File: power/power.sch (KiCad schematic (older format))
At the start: 14 parts, among them P1 CONN_2, P2 CONN_5X2, U1 KPS-5, U2 RB-0515S, U3 RB-0515S, U4 RB-0512D, U5 RB-0505D

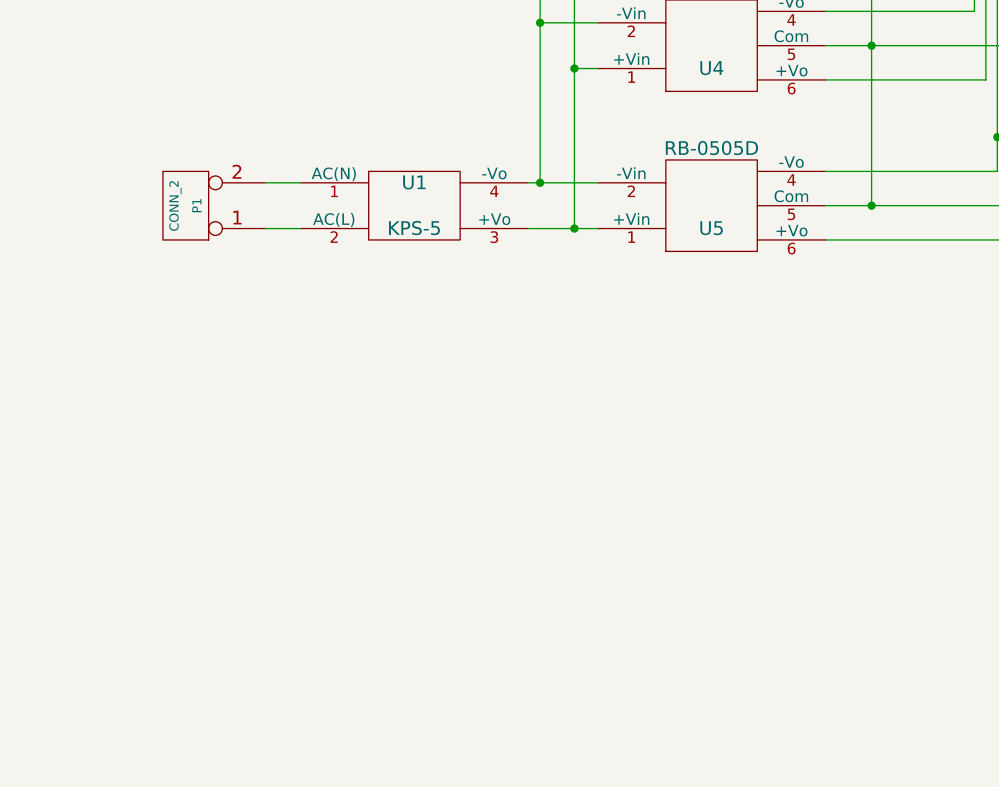
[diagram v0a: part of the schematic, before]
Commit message: [libs, power] dc-dc convertors
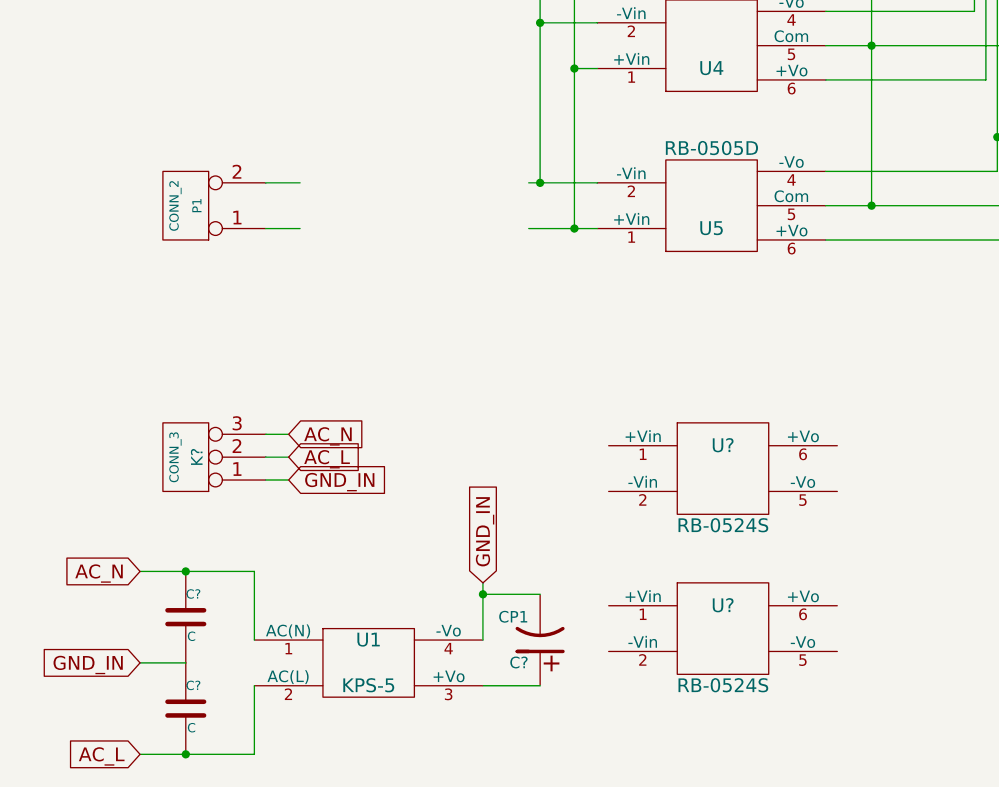
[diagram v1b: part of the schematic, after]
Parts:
- added C? (x2): C, ~, symbol C
- added C?: CP1, ~, symbol CP1
- added K?: CONN_3, ~, symbol CONN_3
- added U? (x2): RB-0524S, ~, symbol RB-0524S
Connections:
- net labels added: AC_L, AC_N, GND_IN
- wire segments 50 -> 61
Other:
- moved on the sheet: U1
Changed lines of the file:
@@
 LIBS:ad8421
 LIBS:ad8067
+LIBS:rb-0524s
 LIBS:power-cache
 EELAYER 27 0
@@
 Sheet 1 1
 Title "Power for PID controller"
-Date "28 jan 2014"
+Date "2 apr 2014"
 Rev ""
 Comp "MIT BEC5"
@@
 L KPS-5 U1
 U 1 1 52E78312
-P 3900 4900
-F 0 "U1" H 3900 5000 60  0000 C CNN
-F 1 "KPS-5" H 3900 4800 60  0000 C CNN
-F 2 "~" H 3900 4900 60  0000 C CNN
-F 3 "~" H 3900 4900 60  0000 C CNN
-	1    3900 4900
+P 3700 6900
+F 0 "U1" H 3700 7000 60  0000 C CNN
+F 1 "KPS-5" H 3700 6800 60  0000 C CNN
+F 2 "~" H 3700 6900 60  0000 C CNN
+F 3 "~" H 3700 6900 60  0000 C CNN
+	1    3700 6900
 	1    0    0    -1
 $EndComp
@@
 NoConn ~ 8400 3900
 NoConn ~ 8400 4000
+$Comp
+L CONN_3 K?
+U 1 1 533AD55D
+P 2900 6000
+F 0 "K?" V 2850 6000 50  0000 C CNN
+F 1 "CONN_3" V 2950 6000 40  0000 C CNN
+F 2 "~" H 2900 6000 60  0000 C CNN
+F 3 "~" H 2900 6000 60  0000 C CNN
+	1    2900 6000
+	-1   0    0    1
+$EndComp
+Text GLabel 3350 5900 2    60   Input ~ 0
+AC_N
+Text GLabel 3350 6000 2    60   Input ~ 0
+AC_L
+Text GLabel 3350 6100 2    60   Input ~ 0
+GND_IN
+Wire Wire Line
+	3250 5900 3350 5900
+Wire Wire Line
+	3250 6000 3350 6000
+Wire Wire Line
+	3250 6100 3350 6100
+Text GLabel 2700 6500 0    60   Input ~ 0
+AC_N
+Text GLabel 2700 7300 0    60   Input ~ 0
+AC_L
+Text GLabel 2700 6900 0    60   Input ~ 0
+GND_IN
+$Comp
+L C C?
+U 1 1 533AD679
+P 2900 6700
+F 0 "C?" H 2900 6800 40  0000 L CNN
+F 1 "C" H 2906 6615 40  0000 L CNN
+F 2 "~" H 2938 6550 30  0000 C CNN
+F 3 "~" H 2900 6700 60  0000 C CNN
+	1    2900 6700
+	1    0    0    -1
+$EndComp
+$Comp
+L C C?
+U 1 1 533AD688
+P 2900 7100
+F 0 "C?" H 2900 7200 40  0000 L CNN
+F 1 "C" H 2906 7015 40  0000 L CNN
+F 2 "~" H 2938 6950 30  0000 C CNN
+F 3 "~" H 2900 7100 60  0000 C CNN
+	1    2900 7100
+	1    0    0    -1
+$EndComp
+Wire Wire Line
+	2700 6900 2900 6900
+Wire Wire Line
+	2700 6500 3200 6500
+Wire Wire Line
+	2700 7300 3200 7300
+Wire Wire Line
+	3200 6500 3200 6800
+Connection ~ 2900 6500
+Wire Wire Line
+	3200 7300 3200 7000
+Connection ~ 2900 7300
+Text GLabel 4200 6550 1    60   Input ~ 0
+GND_IN
+Wire Wire Line
+	4200 6550 4200 6800
+Wire Wire Line
+	4200 7000 4450 7000
+Wire Wire Line
+	4450 6600 4200 6600
+Connection ~ 4200 6600
+$Comp
+L CP1 C?
+U 1 1 533AD9CB
+P 4450 6800
+F 0 "C?" H 4500 6900 50  0000 L CNN
+F 1 "CP1" H 4500 6700 50  0000 L CNN
+F 2 "~" H 4450 6800 60  0000 C CNN
+F 3 "~" H 4450 6800 60  0000 C CNN
+	1    4450 6800
+	-1   0    0    1
+$EndComp
+$Comp
+L RB-0524S U?
+U 1 1 533B760A
+P 5250 6050
+F 0 "U?" H 5250 6150 60  0000 C CNN
+F 1 "RB-0524S" H 5250 5800 60  0000 C CNN
+F 2 "~" H 5250 6050 60  0000 C CNN
+F 3 "~" H 5250 6050 60  0000 C CNN
+	1    5250 6050
+	1    0    0    -1
+$EndComp
+$Comp
+L RB-0524S U?
+U 1 1 533B7617
+P 5250 6750
+F 0 "U?" H 5250 6850 60  0000 C CNN
+F 1 "RB-0524S" H 5250 6500 60  0000 C CNN
+F 2 "~" H 5250 6750 60  0000 C CNN
+F 3 "~" H 5250 6750 60  0000 C CNN
+	1    5250 6750
+	1    0    0    -1
+$EndComp
 $EndSCHEMATC

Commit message: [power] new design
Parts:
- removed C1, C2, C3, C4, C5, C6, C7: CP1, ~, symbol CP1
- removed P1: CONN_2, ~, symbol CONN_2
- removed U2, U3: RB-0515S, ~, symbol RB-0515S
- removed U4: RB-0512D, ~, symbol RB-0512D
- removed U5: RB-0505D, ~, symbol RB-0505D
- removed U? (x2): RB-0524S, ~, symbol RB-0524S
- added C? (x6): 0.022uF, ~, symbol C
- added C? (x9): 330uF, ~, symbol CP1
- added C?: 10uF, ~, symbol CP1
- added C? (x4): 10uF, ~, symbol C
- added C? (x9): C, ~, symbol C
- added C? (x8): 0.01uF, ~, symbol C
- added L? (x14): 10uH, ~, symbol INDUCTOR
- added L? (x5): 470uH, ~, symbol INDUCTOR
- added L? (x5): CIM21J252, ~, symbol INDUCTOR
- added R?: R, ~, symbol R
- added R? (x2): 50k, ~, symbol R
- added R? (x2): 50, ~, symbol R
- added R? (x2): 2k, ~, symbol R
- added R? (x2): 5, ~, symbol R
- added RV? (x4): 10k, ~, symbol POT
- added U? (x2): PDS1-S5-S9-M, ~, symbol PDS1-M-S
- added U? (x2): PDS1-S5-S24-M, ~, symbol PDS1-M-S
- added U? (x2): TPS7A49, ~, symbol TPS7A49
- added U? (x2): TPS7A30, ~, symbol TPS7A30
- C? (x2): value C -> 0.022uF
- C?: value CP1 -> 10uF
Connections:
- net labels added: +20_REG, +24, +7_REG, +9, -20_REG, -24, -7_REG, -9, 0, 0_2, INT+, INT-
- wire segments 61 -> 210
- no-connect marks 3 -> 0
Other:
- moved on the sheet: C?, K?, P2, U1

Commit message: [power] new power board
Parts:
- C11: renamed from C?; value C -> 1uF
- C33, C34, C35, C36, C37, C38, C39, C40: renamed from C?; value C -> 10uF
- R1: renamed from R?; value R -> 0
- gave numbers to parts that had none: 76
- renumbered P2 to P1, U1 to U5
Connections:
- net GND: now reaches L22.2, P1.1, P1.3, P1.5, P1.6, P1.7, P1.9
